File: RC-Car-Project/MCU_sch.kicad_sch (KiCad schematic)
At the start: 16 parts, among them SW1 SW_Push, U7 STM32H743VGTx, Y1 Crystal

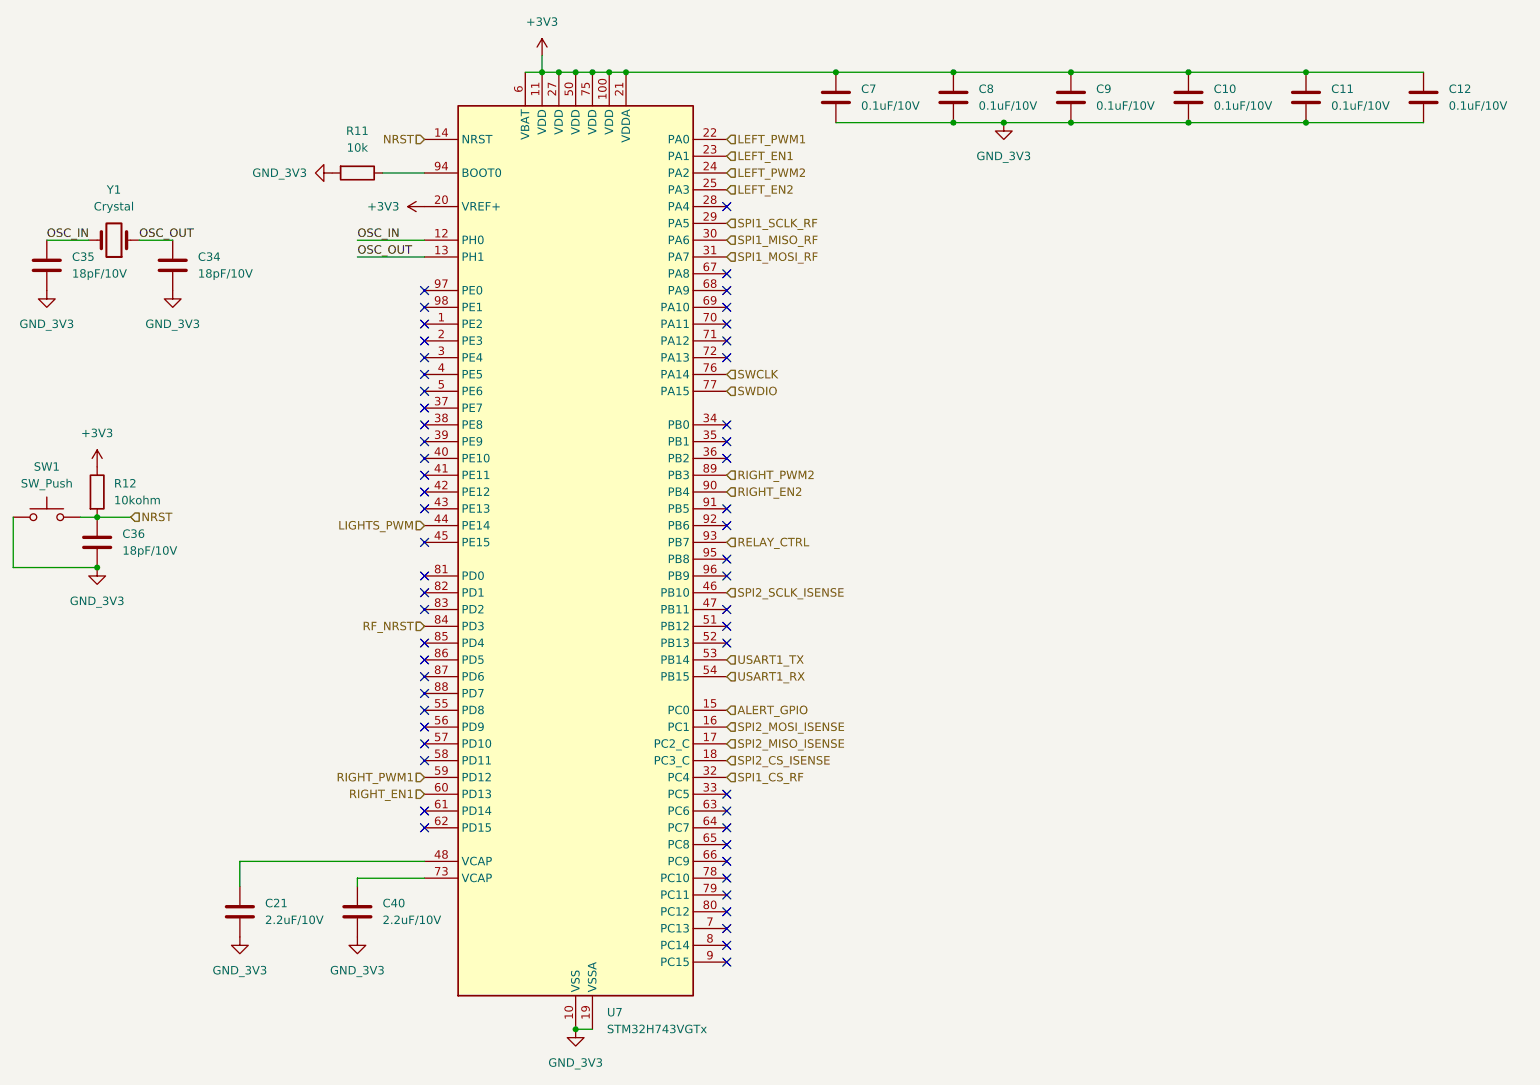
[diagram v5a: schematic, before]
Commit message: Add thermo adc and camera
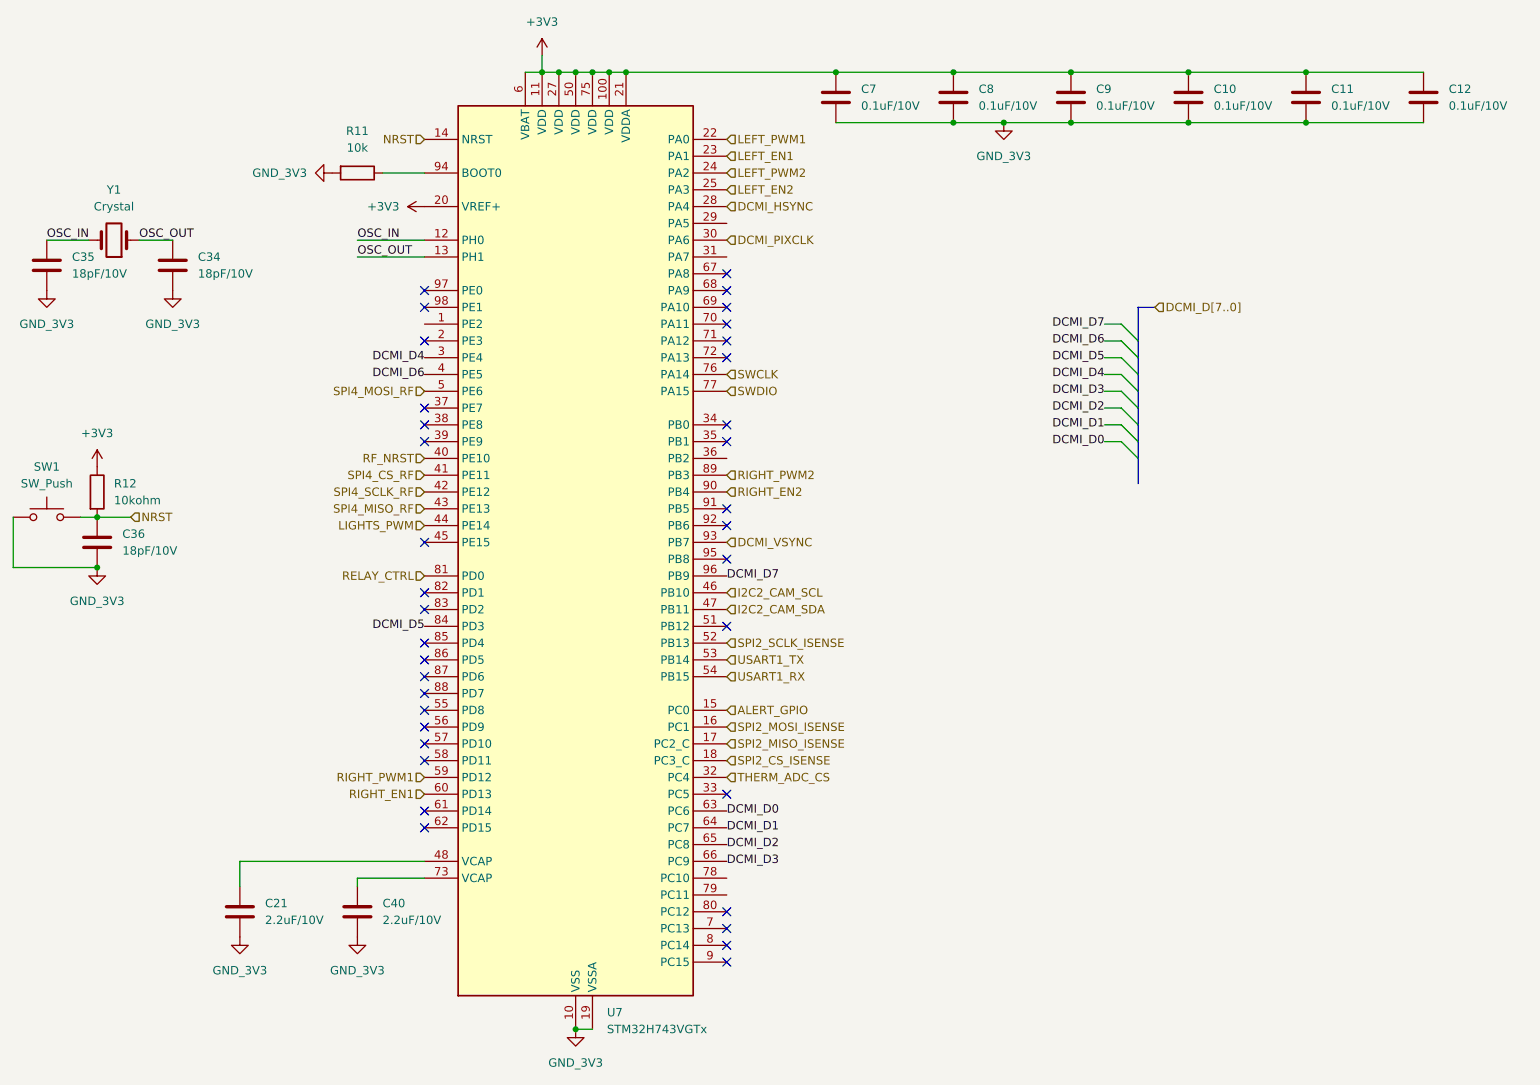
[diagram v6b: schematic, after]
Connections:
- net RELAY_CTRL: now also U7.81 (PD0); no longer U7.93 (PB7)
- net RF_NRST: now also U7.40 (PE10); no longer U7.84 (PD3)
- net SPI2_SCLK_ISENSE: now also U7.52 (PB13); no longer U7.46 (PB10)
- net DCMI_HSYNC: now reaches U7.28 (PA4)
- net DCMI_D4: now reaches U7.3 (PE4)
- net DCMI_D6: now reaches U7.4 (PE5)
- net SPI4_CS_RF: now reaches U7.41 (PE11)
- net SPI4_SCLK_RF: now reaches U7.42 (PE12)
- net SPI4_MISO_RF: now reaches U7.43 (PE13)
- net I2C2_CAM_SDA: now reaches U7.47 (PB11)
- net SPI4_MOSI_RF: now reaches U7.5 (PE6)
- net DCMI_D0: now reaches U7.63 (PC6)
- net DCMI_D1: now reaches U7.64 (PC7)
- net DCMI_D2: now reaches U7.65 (PC8)
- net DCMI_D3: now reaches U7.66 (PC9)
- net DCMI_D7: now reaches U7.96 (PB9)
- net SPI1_CS_RF renamed THERM_ADC_CS
- net SPI1_MISO_RF renamed DCMI_PIXCLK
- net SPI1_MOSI_RF: no longer names the net of U7.31 (PA7)
- net SPI1_SCLK_RF: no longer names the net of U7.29 (PA5)
- new net DCMI_D5: U7.84 (PD3)
- new net DCMI_VSYNC: U7.93 (PB7)
- new net I2C2_CAM_SCL: U7.46 (PB10)
- no-connect marks 56 -> 36

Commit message: Add Camera XCLK
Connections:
- net DCMI_XCLK: now reaches U7.31 (PA7)
- no-connect marks 36 -> 40
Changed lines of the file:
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@@
+	)
+	(no_connect
+		(at 162.56 146.05)
+	)
+	(no_connect
+		(at 116.84 59.69)
 	)
 	(no_connect
@@
 	)
 	(no_connect
+		(at 162.56 143.51)
+	)
+	(no_connect
 		(at 162.56 95.25)
 	)
@@
 	(no_connect
 		(at 162.56 153.67)
+	)
+	(no_connect
+		(at 162.56 44.45)
 	)
 	(no_connect
@@
 		(fields_autoplaced yes)
 		(effects
+			(font
+				(size 1.27 1.27)
+			)
+			(justify left)
+		)
+	)
+	(hierarchical_label "DCMI_XCLK"
+		(shape input)
+		(at 162.56 49.53 0)
+		(fields_autoplaced yes)
+		(effects

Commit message: Fixed Drivers
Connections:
- net LIGHTS2_PWM: now reaches U7.34 (PB0)
- net LEFT_EN1 renamed MOTOR_EN
- net LEFT_EN2: no longer names the net of U7.25 (PA3)
- net LIGHTS_PWM renamed LIGHTS1_PWM
- net RELAY_CTRL: no longer names the net of U7.81 (PD0)
- net RIGHT_EN1: no longer names the net of U7.60 (PD13)
- net RIGHT_EN2: no longer names the net of U7.90 (PB4)
- no-connect marks 40 -> 44
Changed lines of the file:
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@@
-	)
-	(no_connect
-		(at 162.56 74.93)
 	)
 	(no_connect
@@
 	)
 	(no_connect
+		(at 162.56 39.37)
+	)
+	(no_connect
 		(at 116.84 102.87)
 	)
 	(no_connect
+		(at 116.84 97.79)
+	)
+	(no_connect
 		(at 116.84 57.15)
 	)
@@
 	)
 	(no_connect
+		(at 162.56 85.09)
+	)
+	(no_connect
+		(at 162.56 80.01)
+	)
+	(no_connect
 		(at 162.56 95.25)
 	)
@@
 	(no_connect
 		(at 116.84 92.71)
+	)
+	(no_connect
+		(at 116.84 130.81)
 	)
 	(no_connect
@@
 		)
 	)
-	(hierarchical_label "RELAY_CTRL"
-		(shape input)
-		(at 116.84 97.79 180)
-		(fields_autoplaced yes)
-		(effects
-			(font
-				(size 1.27 1.27)
-			)
-			(justify right)
-		)
-	)
 	(hierarchical_label "DCMI_D[7..0]"
 		(shape input)
@@
 		)
 	)
-	(hierarchical_label "RIGHT_EN2"
-		(shape input)
-		(at 162.56 85.09 0)
-		(fields_autoplaced yes)
-		(effects
-			(font
-				(size 1.27 1.27)
-			)
-			(justify left)
-		)
-	)
 	(hierarchical_label "LEFT_PWM2"
 		(shape input)
@@
 		)
 	)
-	(hierarchical_label "LEFT_EN2"
-		(shape input)
-		(at 162.56 39.37 0)
+	(hierarchical_label "LIGHTS2_PWM"
+		(shape input)
+		(at 162.56 74.93 0)
 		(fields_autoplaced yes)
 		(effects
@@
 		)
 	)
-	(hierarchical_label "LIGHTS_PWM"
+	(hierarchical_label "LIGHTS1_PWM"
 		(shape input)
 		(at 116.84 90.17 180)
@@
 		)
 	)
-	(hierarchical_label "LEFT_EN1"
+	(hierarchical_label "MOTOR_EN"
 		(shape input)
 		(at 162.56 34.29 0)
@@
 		(fields_autoplaced yes)
 		(effects
-			(font
-				(size 1.27 1.27)
-			)
-			(justify right)
-		)
-	)
-	(hierarchical_label "RIGHT_EN1"
-		(shape input)
-		(at 116.84 130.81 180)
-		(fields_autoplaced yes)
-		(effects
